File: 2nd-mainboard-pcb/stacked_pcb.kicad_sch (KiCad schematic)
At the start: 16 parts, among them J12 Steckverbinder_Male_Fans, J13 Steckverbinder_Female_Leistung, J15 Steckverbinder_Female_Motoren, J24 Steckverbinder_Male_Leistung

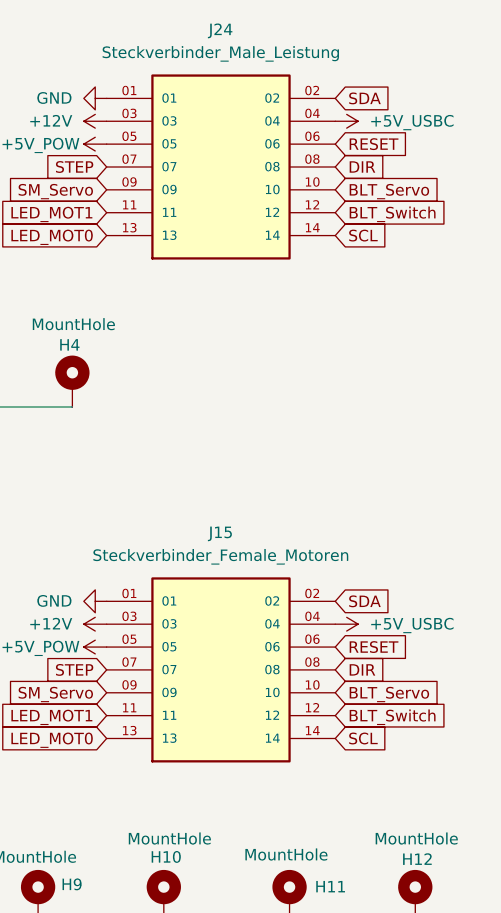
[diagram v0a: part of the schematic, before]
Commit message: stacked design verbessert, power plane aufgeteilt
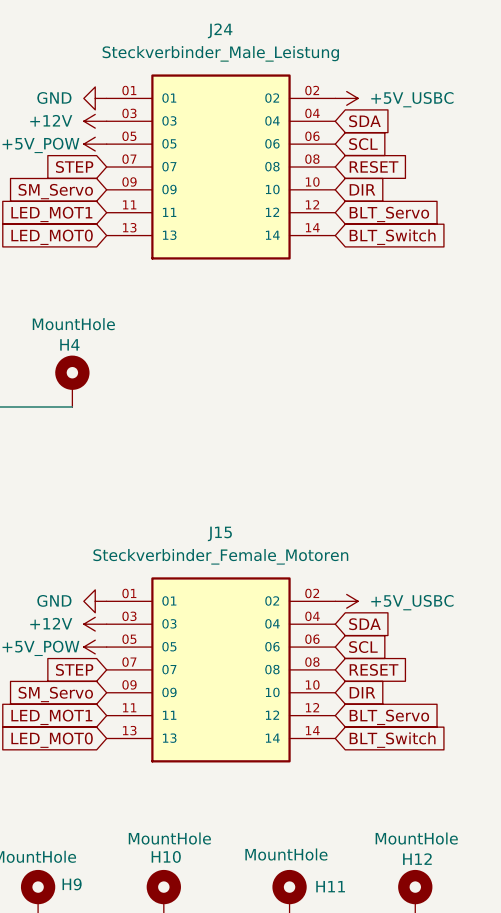
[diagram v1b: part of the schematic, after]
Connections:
- net +5V_USBC: now also J15.02, J24.02; no longer J15.04, J24.04
- net BLT_Servo: now also J15.12, J24.12; no longer J15.10, J24.10
- net BLT_Switch: now also J15.14, J24.14; no longer J15.12, J24.12
- net DIR: now also J15.10, J24.10; no longer J15.08, J24.08
- net RESET: now also J15.08, J24.08; no longer J15.06, J24.06
- net SCL: now also J15.06, J24.06; no longer J15.14, J24.14
- net SDA: now also J15.04, J24.04; no longer J15.02, J24.02
